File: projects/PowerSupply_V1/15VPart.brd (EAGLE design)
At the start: 49.5 x 58.4 mm, 24 parts, among them IC1 LM2596T, IC2 LM2596T, X1 IN, X2 OUT

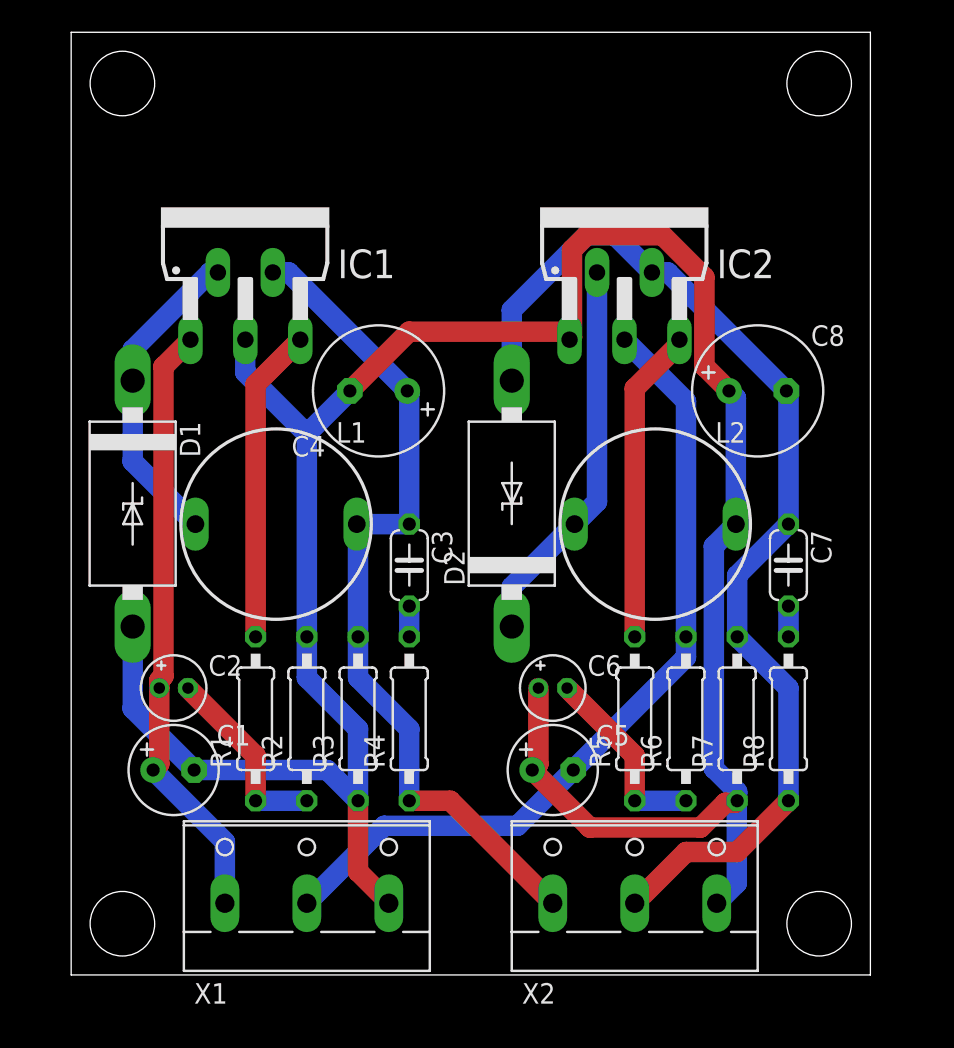
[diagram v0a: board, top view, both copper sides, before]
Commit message: refactor(15v): schematics and routing changed
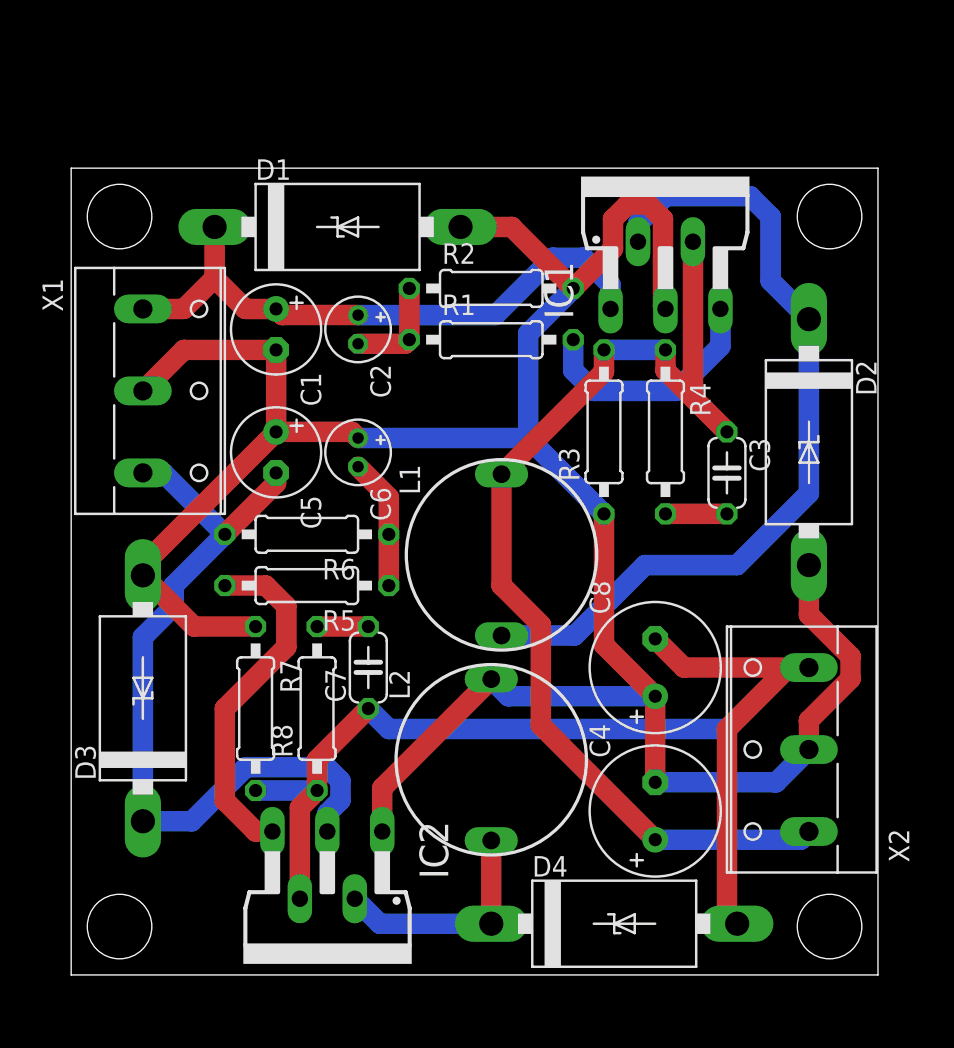
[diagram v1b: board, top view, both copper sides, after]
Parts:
- added D3, D4: 1N5822, diode:C4111-15
- C4: value 220µF -> 330µF
- C8: value 330µF -> 470µF
- moved IC2 44.6 mm to (15.9, 3.81), turned to 180 degrees
- moved X1 32.5 mm to (5.08, 36.2), turned to 270 degrees
- moved C4 31.2 mm to (36.2, 10.2), turned to 90 degrees
- moved R7 29.9 mm to (11.4, 16.5), turned to 270 degrees
- moved R8 29.2 mm to (15.2, 16.5)
- moved R2 29.0 mm to (26.0, 42.5), turned to 0 degrees
- moved C1 28.0 mm to (12.7, 40.0), turned to 270 degrees
- moved R1 27.7 mm to (26.0, 39.4), turned to 0 degrees
- moved C7 26.8 mm to (18.4, 19.1), turned to 90 degrees
- moved R6 26.1 mm to (14.6, 27.3), turned to 180 degrees
- moved C5 26.1 mm to (12.7, 32.4), turned to 270 degrees
- moved IC1 26.1 mm to (36.8, 46.4)
- moved C2 25.0 mm to (17.8, 40.0), turned to 270 degrees
- moved R4 23.8 mm to (36.8, 33.7), turned to 270 degrees
- moved R3 23.4 mm to (33.0, 33.7)
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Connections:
- net +24V: now also D1.C
- net -15V: now also D4.A, X2.3; no longer D2.A, X2.2
- net -24V: now also D3.C, X1.3; no longer X1.2
- net GND: now also D2.A, D3.A, X1.2, X2.2; no longer X1.3, X2.3
- net N$2: now also D4.C; no longer D2.C
- net N$3: now also D2.C; no longer D1.C
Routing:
- net N$3: track 19.7 -> 51.4 mm
- net +15V: track 52.9 -> 69.8 mm
- net N$2: track 24.1 -> 14.3 mm
- net -15V: track 67.6 -> 76.0 mm
- net N$6: track 11.9 -> 6.46 mm
- net N$4: track 19.6 -> 15.0 mm
- net N$8: track 11.9 -> 8.16 mm
- net N$7: track 19.6 -> 21.7 mm
- net -24V: track 51.1 -> 49.1 mm
- net N$1: track 1.91 -> 3.81 mm
- net N$5: track 1.91 -> 3.17 mm
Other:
- board size 49.5 x 58.4 mm -> 50 x 50 mm

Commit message: feat: 15VPart refactored
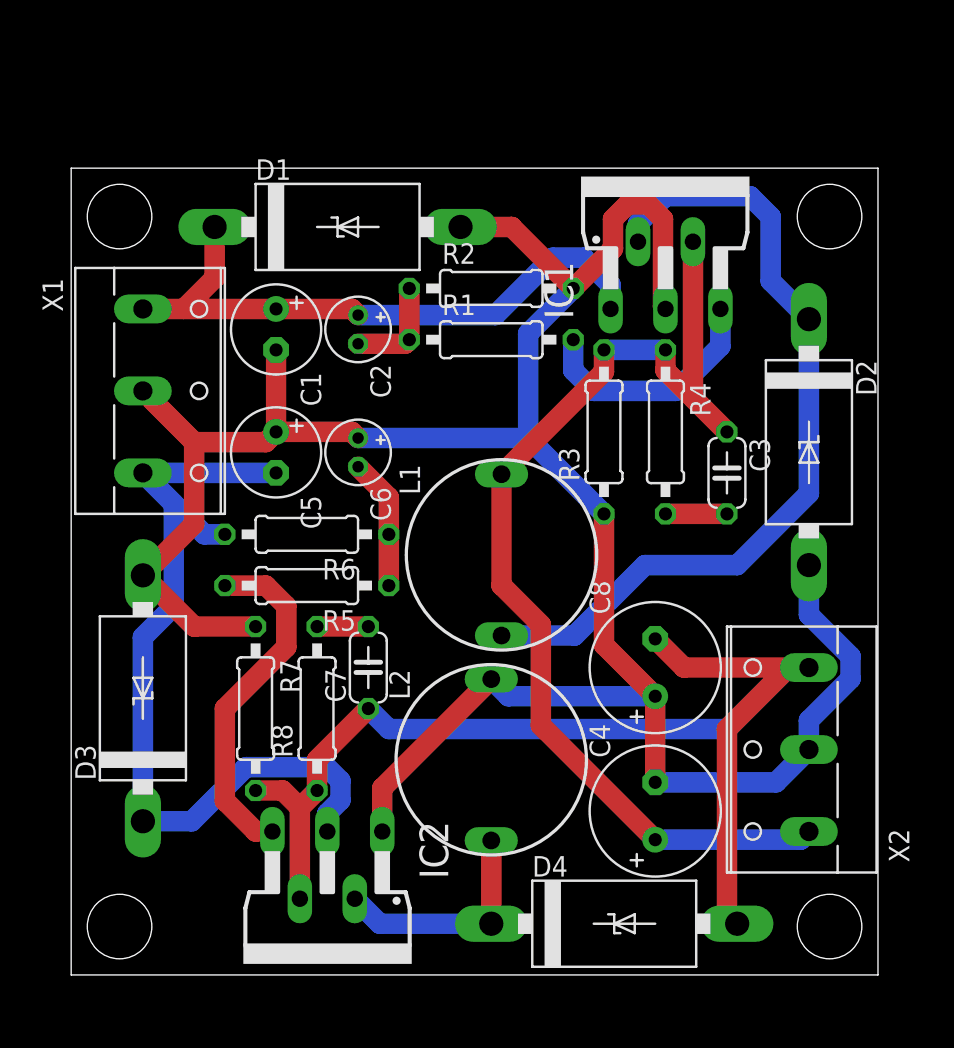
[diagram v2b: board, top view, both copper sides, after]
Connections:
- net +24V renamed +20V
- net -24V renamed -20V
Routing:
- net -20V: track 49.1 -> 55.5 mm
- net -15V: track 76.0 -> 74.1 mm
- net GND: track 155.9 -> 154.4 mm

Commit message: feat: small fixes and changes applied
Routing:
- net GND: track 154.4 -> 153.7 mm
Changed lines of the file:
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@@
 <setting verticaltext="up"/>
 </settings>
-<grid distance="25" unitdist="mil" unit="mil" style="lines" multiple="1" display="yes" altdistance="5" altunitdist="mil" altunit="mil"/>
+<grid distance="25" unitdist="mil" unit="mm" style="lines" multiple="1" display="yes" altdistance="5" altunitdist="mil" altunit="mm"/>
 <layers>
 <layer number="1" name="Top" color="4" fill="1" visible="yes" active="yes"/>
@@
 </element>
 <element name="D2" library="diode" library_urn="urn:adsk.eagle:library:210" package="C4111-15" package3d_urn="urn:adsk.eagle:package:43355/2" value="1N5822" x="45.72" y="33.02" smashed="yes" rot="R270">
-<attribute name="NAME" x="48.641" y="38.1" size="1.27" layer="25" ratio="10" rot="R270"/>
+<attribute name="NAME" x="47.371" y="40.64" size="1.27" layer="25" ratio="10" rot="R270"/>
 <attribute name="POPULARITY" value="0" x="16.51" y="-12.7" size="1.778" layer="27" rot="R270" display="off"/>
 <attribute name="VALUE" x="43.561" y="35.56" size="1.27" layer="27" ratio="10" rot="R270"/>
@@
 </element>
 <element name="D1" library="diode" library_urn="urn:adsk.eagle:library:210" package="C4111-15" package3d_urn="urn:adsk.eagle:package:43355/2" value="1N5822" x="16.51" y="46.355" smashed="yes">
-<attribute name="NAME" x="11.43" y="49.276" size="1.27" layer="25" ratio="10"/>
+<attribute name="NAME" x="8.89" y="48.006" size="1.27" layer="25" ratio="10"/>
 <attribute name="POPULARITY" value="0" x="59.69" y="8.255" size="1.778" layer="27" display="off"/>
 <attribute name="VALUE" x="13.97" y="44.196" size="1.27" layer="27" ratio="10"/>
 </element>
 <element name="D3" library="diode" library_urn="urn:adsk.eagle:library:210" package="C4111-15" package3d_urn="urn:adsk.eagle:package:43355/2" value="1N5822" x="4.445" y="17.145" smashed="yes" rot="R90">
-<attribute name="NAME" x="1.524" y="12.065" size="1.27" layer="25" ratio="10" rot="R90"/>
+<attribute name="NAME" x="2.794" y="9.525" size="1.27" layer="25" ratio="10" rot="R90"/>
 <attribute name="POPULARITY" value="0" x="50.165" y="40.005" size="1.778" layer="27" rot="R90" display="off"/>
 <attribute name="VALUE" x="6.604" y="14.605" size="1.27" layer="27" ratio="10" rot="R90"/>
@@
 <attribute name="MF" value="" x="83.82" y="38.735" size="1.778" layer="27" display="off"/>
 <attribute name="MPN" value="LM2596T-ADJ/LF02" x="83.82" y="38.735" size="1.778" layer="27" display="off"/>
-<attribute name="NAME" x="31.115" y="40.64" size="1.778" layer="25" ratio="10" rot="R90"/>
+<attribute name="NAME" x="41.275" y="42.545" size="1.778" layer="25" ratio="10"/>
 <attribute name="OC_FARNELL" value="9494162" x="83.82" y="38.735" size="1.778" layer="27" display="off"/>
 <attribute name="OC_NEWARK" value="65K5910" x="83.82" y="38.735" size="1.778" layer="27" display="off"/>
 <attribute name="POPULARITY" value="0" x="83.82" y="38.735" size="1.778" layer="27" display="off"/>
-<attribute name="VALUE" x="44.45" y="40.64" size="1.778" layer="27" ratio="10" rot="R90"/>
+<attribute name="VALUE" x="21.59" y="47.625" size="1.778" layer="27" ratio="10"/>
 </element>
 <element name="IC2" library="national-semiconductor" library_urn="urn:adsk.eagle:library:307" package="T05D" package3d_urn="urn:adsk.eagle:package:21216/1" value="LM2596T" x="15.875" y="3.81" smashed="yes" rot="R180">
 <attribute name="MF" value="" x="-5.715" y="24.13" size="1.778" layer="27" rot="R180" display="off"/>
 <attribute name="MPN" value="LM2596T-ADJ/LF02" x="-5.715" y="24.13" size="1.778" layer="27" rot="R180" display="off"/>
-<attribute name="NAME" x="21.59" y="9.525" size="1.778" layer="25" ratio="10" rot="R270"/>
+<attribute name="NAME" x="20.32" y="5.715" size="1.778" layer="25" ratio="10"/>
 <attribute name="OC_FARNELL" value="9494162" x="-5.715" y="24.13" size="1.778" layer="27" rot="R180" display="off"/>
 <attribute name="OC_NEWARK" value="65K5910" x="-5.715" y="24.13" size="1.778" layer="27" rot="R180" display="off"/>
 <attribute name="POPULARITY" value="0" x="-5.715" y="24.13" size="1.778" layer="27" rot="R180" display="off"/>
-<attribute name="VALUE" x="8.255" y="9.525" size="1.778" layer="27" ratio="10" rot="R270"/>
+<attribute name="VALUE" x="1.27" y="5.715" size="1.778" layer="27" ratio="10"/>
 </element>
 <element name="L1" library="inductor-neosid" library_urn="urn:adsk.eagle:library:241" package="SD12-680" package3d_urn="urn:adsk.eagle:package:14657/1" value="33µH" x="26.67" y="26.035" smashed="yes" rot="R90">
 <attribute name="MF" value="BUSSMANN" x="33.02" y="45.085" size="1.778" layer="27" rot="R90" display="off"/>
 <attribute name="MPN" value="SD12-680" x="33.02" y="45.085" size="1.778" layer="27" rot="R90" display="off"/>
-<attribute name="NAME" x="21.622" y="29.762" size="1.27" layer="25" rot="R90"/>
+<attribute name="NAME" x="24.797" y="24.682" size="1.27" layer="25" rot="R90"/>
 <attribute name="OC_FARNELL" value="unknown" x="33.02" y="45.085" size="1.778" layer="27" rot="R90" display="off"/>
 <attribute name="OC_NEWARK" value="19K7201" x="33.02" y="45.085" size="1.778" layer="27" rot="R90" display="off"/>
 <attribute name="POPULARITY" value="0" x="33.02" y="45.085" size="1.778" layer="27" rot="R90" display="off"/>
-<attribute name="VALUE" x="29.67" y="22.785" size="1.27" layer="27" rot="R90"/>
+<attribute name="VALUE" x="29.67" y="23.42" size="1.27" layer="27" rot="R90"/>
 </element>
 <element name="L2" library="inductor-neosid" library_urn="urn:adsk.eagle:library:241" package="SD12-680" package3d_urn="urn:adsk.eagle:package:14657/1" value="47µH" x="26.035" y="13.335" smashed="yes" rot="R90">
 <attribute name="MF" value="BUSSMANN" x="32.385" y="45.085" size="1.778" layer="27" rot="R90" display="off"/>
 <attribute name="MPN" value="SD12-680" x="32.385" y="45.085" size="1.778" layer="27" rot="R90" display="off"/>
-<attribute name="NAME" x="20.987" y="17.062" size="1.27" layer="25" rot="R90"/>
+<attribute name="NAME" x="24.162" y="11.982" size="1.27" layer="25" rot="R90"/>
 <attribute name="OC_FARNELL" value="unknown" x="32.385" y="45.085" size="1.778" layer="27" rot="R90" display="off"/>
 <attribute name="OC_NEWARK" value="19K7201" x="32.385" y="45.085" size="1.778" layer="27" rot="R90" display="off"/>
 <attribute name="POPULARITY" value="0" x="32.385" y="45.085" size="1.778" layer="27" rot="R90" display="off"/>
-<attribute name="VALUE" x="29.035" y="10.085" size="1.27" layer="27" rot="R90"/>
+<attribute name="VALUE" x="29.035" y="10.72" size="1.27" layer="27" rot="R90"/>
 </element>
 <element name="R1" library="rcl" library_urn="urn:adsk.eagle:library:334" package="0207/10" package3d_urn="urn:adsk.eagle:package:23491/2" value="47k" x="26.035" y="39.37" smashed="yes">
@@
 <attribute name="MF" value="" x="-16.51" y="-1.905" size="1.778" layer="27" rot="R270" display="off"/>
 <attribute name="MPN" value="" x="-16.51" y="-1.905" size="1.778" layer="27" rot="R270" display="off"/>
-<attribute name="NAME" x="-1.778" y="43.18" size="1.27" layer="25" ratio="10" rot="R270"/>
+<attribute name="NAME" x="0.762" y="31.115" size="1.27" layer="25" ratio="10" rot="R270"/>
 <attribute name="OC_FARNELL" value="unknown" x="-16.51" y="-1.905" size="1.778" layer="27" rot="R270" display="off"/>
 <attribute name="OC_NEWARK" value="unknown" x="-16.51" y="-1.905" size="1.778" layer="27" rot="R270" display="off"/>
 <attribute name="POPULARITY" value="3" x="-16.51" y="-1.905" size="1.778" layer="27" rot="R270" display="off"/>
-<attribute name="VALUE" x="0.762" y="42.799" size="1.27" layer="27" ratio="10" rot="R270"/>
+<attribute name="VALUE" x="0.762" y="43.434" size="1.27" layer="27" ratio="10" rot="R270"/>
 </element>
 <element name="X2" library="con-wago-508" library_urn="urn:adsk.eagle:library:196" package="W237-133" package3d_urn="urn:adsk.eagle:package:10737/1" value="OUT" x="45.085" y="13.97" smashed="yes" rot="R90">
 <attribute name="MF" value="" x="66.675" y="68.58" size="1.778" layer="27" rot="R90" display="off"/>
 <attribute name="MPN" value="" x="66.675" y="68.58" size="1.778" layer="27" rot="R90" display="off"/>
-<attribute name="NAME" x="51.943" y="6.985" size="1.27" layer="25" ratio="10" rot="R90"/>
+<attribute name="NAME" x="49.403" y="19.05" size="1.27" layer="25" ratio="10" rot="R90"/>
 <attribute name="OC_FARNELL" value="unknown" x="66.675" y="68.58" size="1.778" layer="27" rot="R90" display="off"/>
 <attribute name="OC_NEWARK" value="unknown" x="66.675" y="68.58" size="1.778" layer="27" rot="R90" display="off"/>
 <attribute name="POPULARITY" value="3" x="66.675" y="68.58" size="1.778" layer="27" rot="R90" display="off"/>
-<attribute name="VALUE" x="49.403" y="7.366" size="1.27" layer="27" ratio="10" rot="R90"/>
+<attribute name="VALUE" x="49.403" y="6.731" size="1.27" layer="27" ratio="10" rot="R90"/>
 </element>
 </elements>
@@
 <contactref element="X2" pad="2"/>
 <contactref element="X1" pad="2"/>
-<wire x1="4.445" y1="25.4" x2="4.445" y2="24.765" width="1.27" layer="1"/>
 <wire x1="4.445" y1="24.765" x2="7.62" y2="21.59" width="1.27" layer="1"/>
 <wire x1="7.62" y1="21.59" x2="11.43" y2="21.59" width="1.27" layer="1"/>
